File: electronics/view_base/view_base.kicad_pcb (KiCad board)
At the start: 2 copper layers, 81.2 x 81.2 mm, 106 parts, among them J1 BLDC, J2 USB_C_Receptacle_USB2.0, J3 LCD, J4 A, J5 B, Q1 MMBT4403, Q2 UMH3N, U1 MT6701-CT, U2 T-Micro32_Plus, U3 CH340C, U4 HX711, U5 TMC6300, U6 AP2114HA-3.3, U7 SN74LV1T34DBV, U8 VEML7700

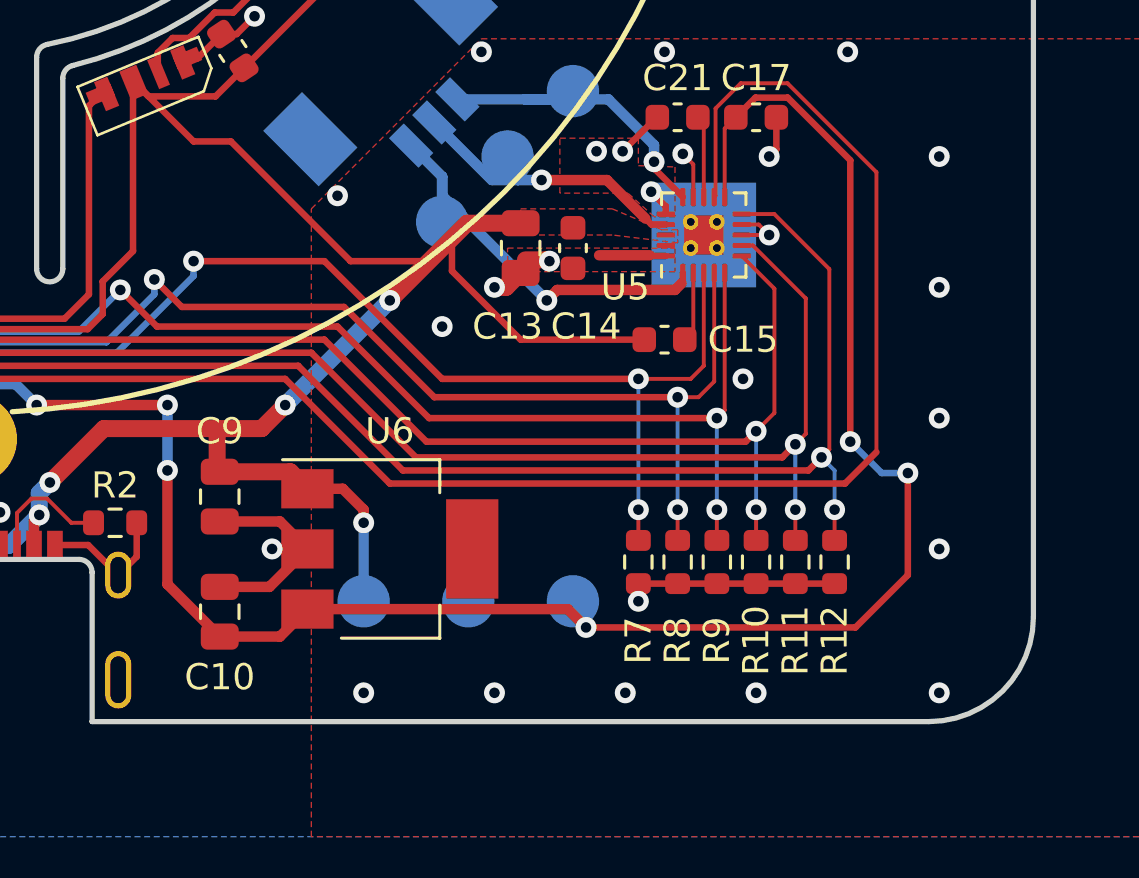
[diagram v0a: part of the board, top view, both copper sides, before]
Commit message: Adding second footprint for 3V3 voltage regulator (#98)
The voltage regulator that was originally used isn't available at the moment. To provide more options, a second footprint was added to the PCB for an alternative regulator that has a different pinout. Important to note that only one regulator should be used.

Also, adjusted .gitignore for Mac files and KiCad auto-generated backups.
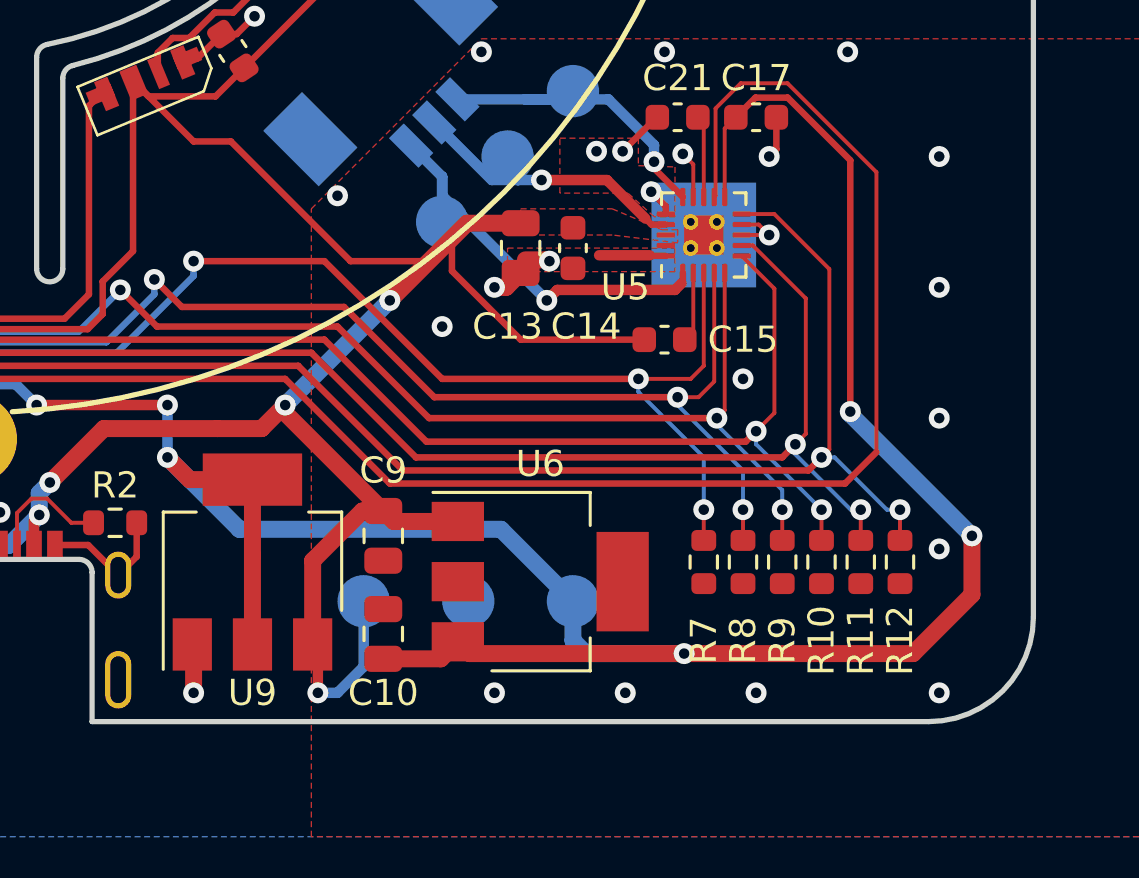
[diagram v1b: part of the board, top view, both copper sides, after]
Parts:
- added U9: TS1117BCW33_RPG, Package_TO_SOT_SMD:SOT-223-3_TabPin2, F.Cu at (110.8, 134.5)
- moved C9 6.43 mm to (115.8, 133.5)
- moved C10 6.31 mm to (115.8, 137.2)
- moved U6 5.88 mm to (121.8, 135.2)
- moved R10 2.50 mm to (132.5, 134.5)
- moved R11 2.50 mm to (134.0, 134.5)
- moved R12 2.50 mm to (135.5, 134.5)
- moved R7 2.50 mm to (128.0, 134.5)
- moved R8 2.50 mm to (129.5, 134.5)
- moved R9 2.50 mm to (131.0, 134.5)
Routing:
- net +3V3: track 315.6 -> 337.6 mm
- net GND: track 86.3 -> 70.9 mm, vias 49 -> 47
- net +5V: track 251.2 -> 261.8 mm
- net /TMC_VL: track 73.2 -> 74.8 mm
- net /TMC_WL: track 69.8 -> 71.0 mm
- net /TMC_WH: track 66.6 -> 67.6 mm
- net /TMC_VH: track 65.8 -> 66.9 mm
- net /TMC_UL: track 67.0 -> 68.0 mm
- net /TMC_UH: track 65.7 -> 66.7 mm

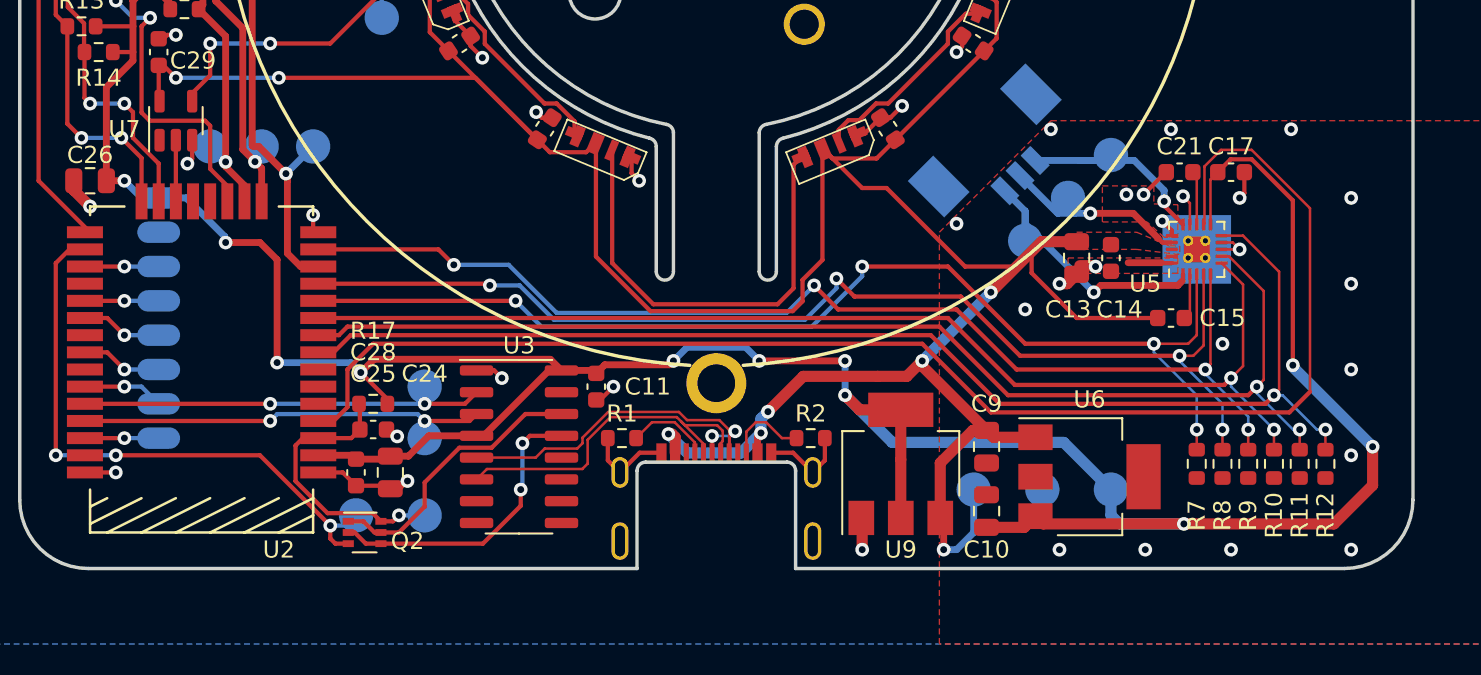
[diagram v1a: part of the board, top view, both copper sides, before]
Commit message: Add BOM entries and note for new LDO
Also clean up PCB:
- Make LDOs mirror each other on board
- Custom footprints with silkscreen "in" "gnd" "out" labels
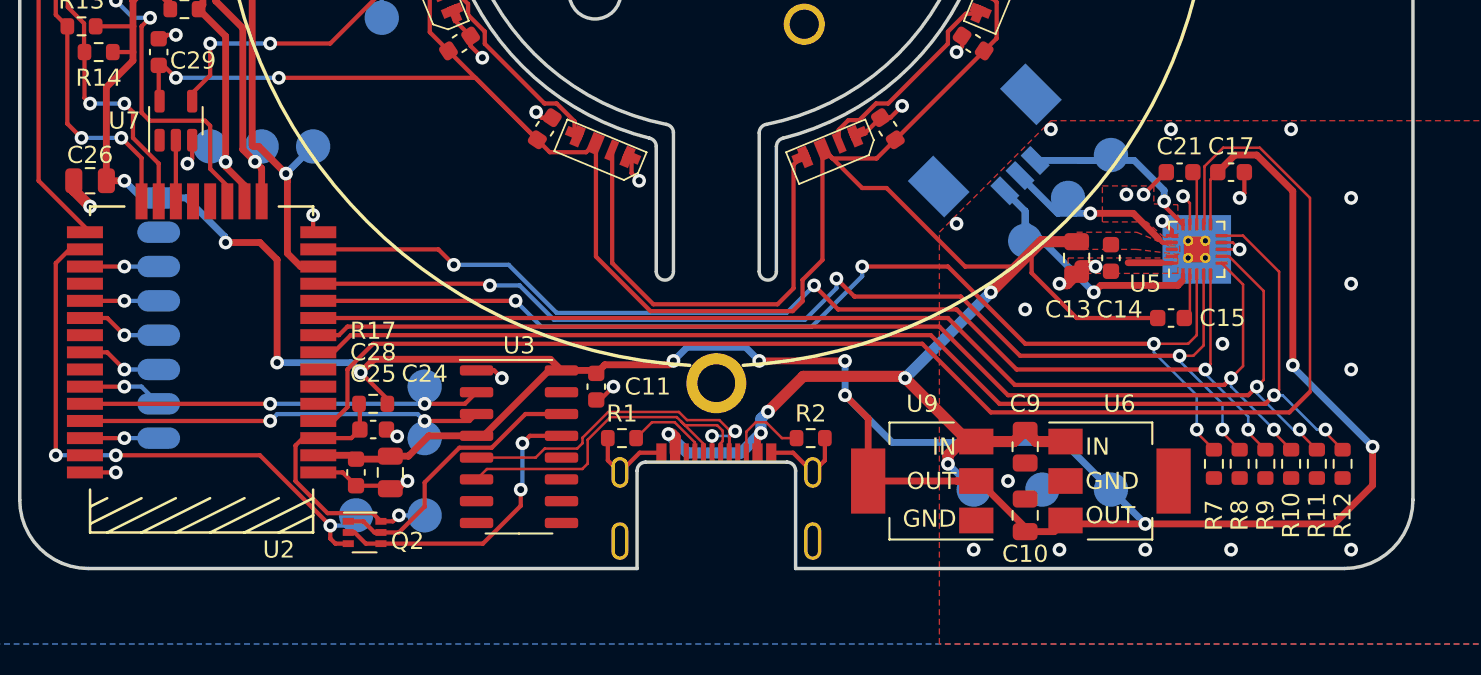
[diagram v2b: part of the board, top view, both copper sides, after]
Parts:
- U6: footprint Package_TO_SOT_SMD:SOT-223-3_TabPin2 -> Modified:SOT-223-3_TabPin2_InGndOut
- U9: footprint Package_TO_SOT_SMD:SOT-223-3_TabPin2 -> Modified:SOT-223-3_TabPin2_GndOutIn
- moved C10 2.26 mm to (118.0, 137.5)
- moved C9 2.25 mm to (118.0, 133.5)
- moved U6 1.77 mm to (123.5, 135.5)
- moved U9 1.60 mm to (112.0, 135.5), turned to 180 degrees
- moved R10 1.00 mm to (133.5, 134.5)
- moved R11 1.00 mm to (135.0, 134.5)
- moved R12 1.00 mm to (136.5, 134.5)
- moved R7 1.00 mm to (129.0, 134.5)
- moved R8 1.00 mm to (130.5, 134.5)
- moved R9 1.00 mm to (132.0, 134.5)
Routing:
- net +5V: track 261.8 -> 256.1 mm
- net +3V3: track 337.6 -> 340.1 mm
- net GND: track 70.9 -> 69.1 mm

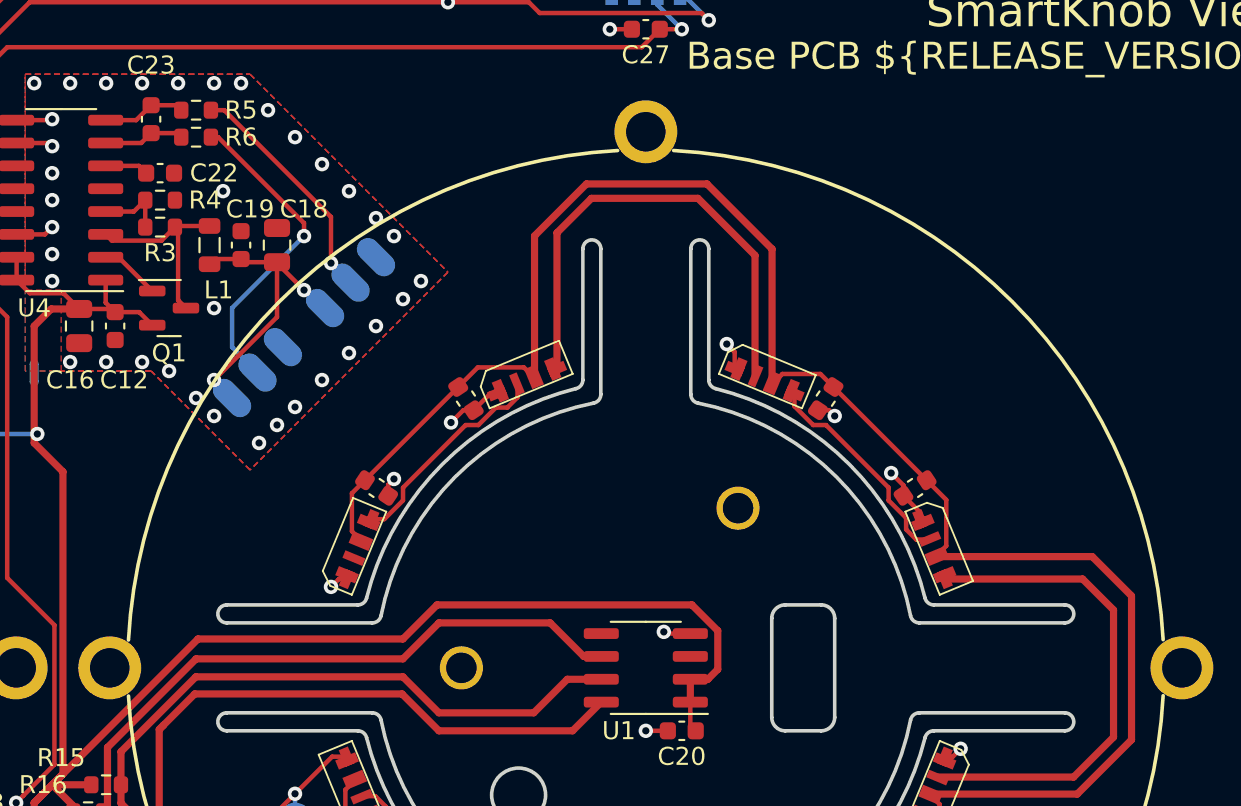
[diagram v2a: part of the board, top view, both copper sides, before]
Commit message: Use 2512 SMD resistors in place of strain gauges (#104)
As suggested in https://github.com/scottbez1/smartknob/issues/24#issuecomment-1073540944 and inspired by https://github.com/IvDm/Z-probe-on-smd-resistors-2512, this adds 4x 330 ohm 2512 SMD resistors to the back to act as strain gauges, rather than requiring discrete strain gauges to be glued and wired up.

Also applies a few changes I accidentally had pending locally:
- Custom footprints for the 2 3.3v LDO options to clarify the pinout options
![image](https://user-images.githubusercontent.com/414890/204078474-8327e8ed-78b5-4fe3-a91d-9c20fe54fcbc.png)
- some BOM note updates

Fixes #24
Closes #33
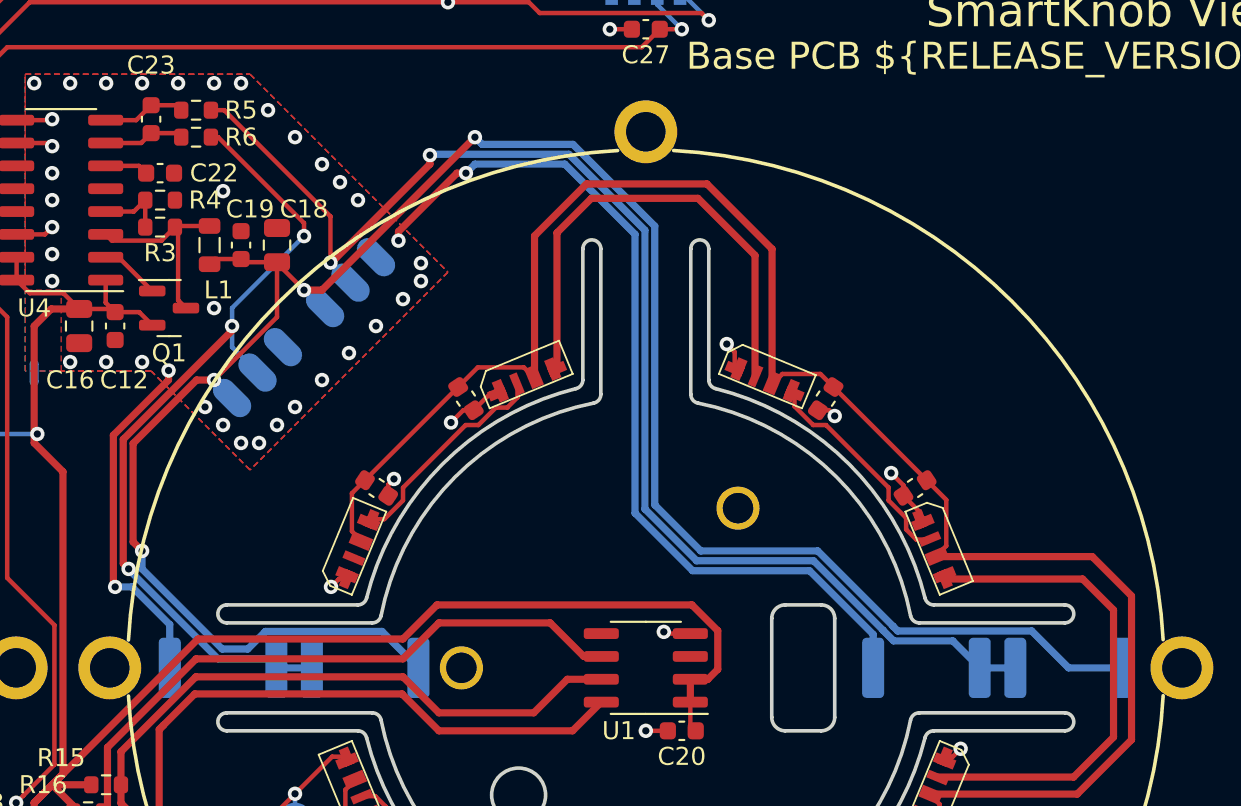
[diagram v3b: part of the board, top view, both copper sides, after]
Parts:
- removed Z1, Z2, Z3, Z4: BF350-3AA Strain Gauge, strain:BF350-3AA
- added R18: 330, Resistor_SMD:R_2512_6332Metric, B.Cu at (123.5, 100.0)
- added R19: 330, Resistor_SMD:R_2512_6332Metric, B.Cu at (115.6, 100.0)
- added R20: 330, Resistor_SMD:R_2512_6332Metric, B.Cu at (84.4, 100.0)
- added R21: 330, Resistor_SMD:R_2512_6332Metric, B.Cu at (76.5, 100.0)
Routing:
- net /STRAIN_E+: track 17.1 -> 119.0 mm, vias 2 -> 4
- net GNDA: track 6.19 -> 76.1 mm, vias 36 -> 40
- net /STRAIN_S+: track 13.2 -> 75.0 mm, vias 1 -> 2
- net /STRAIN_S-: track 17.7 -> 46.3 mm, vias 1 -> 3
